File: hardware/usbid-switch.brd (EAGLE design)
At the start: 33 x 22.9 mm, 5 parts, among them J1 USB-MICRO-ZX80-B-5S, J2 USB-MICRO-105133-0011, SW1 SWITCH-SPDT-EG1215

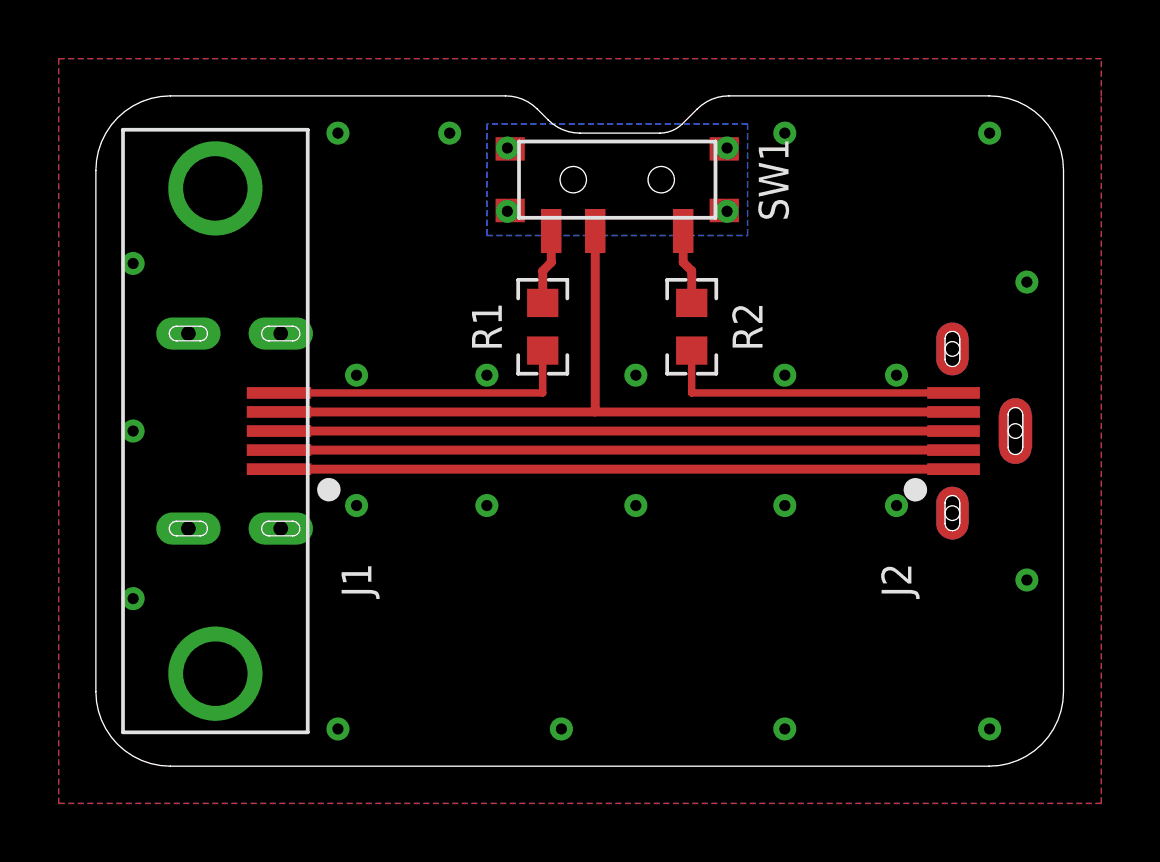
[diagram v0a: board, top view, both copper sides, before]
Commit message: Updated BOM attributes for currently available parts
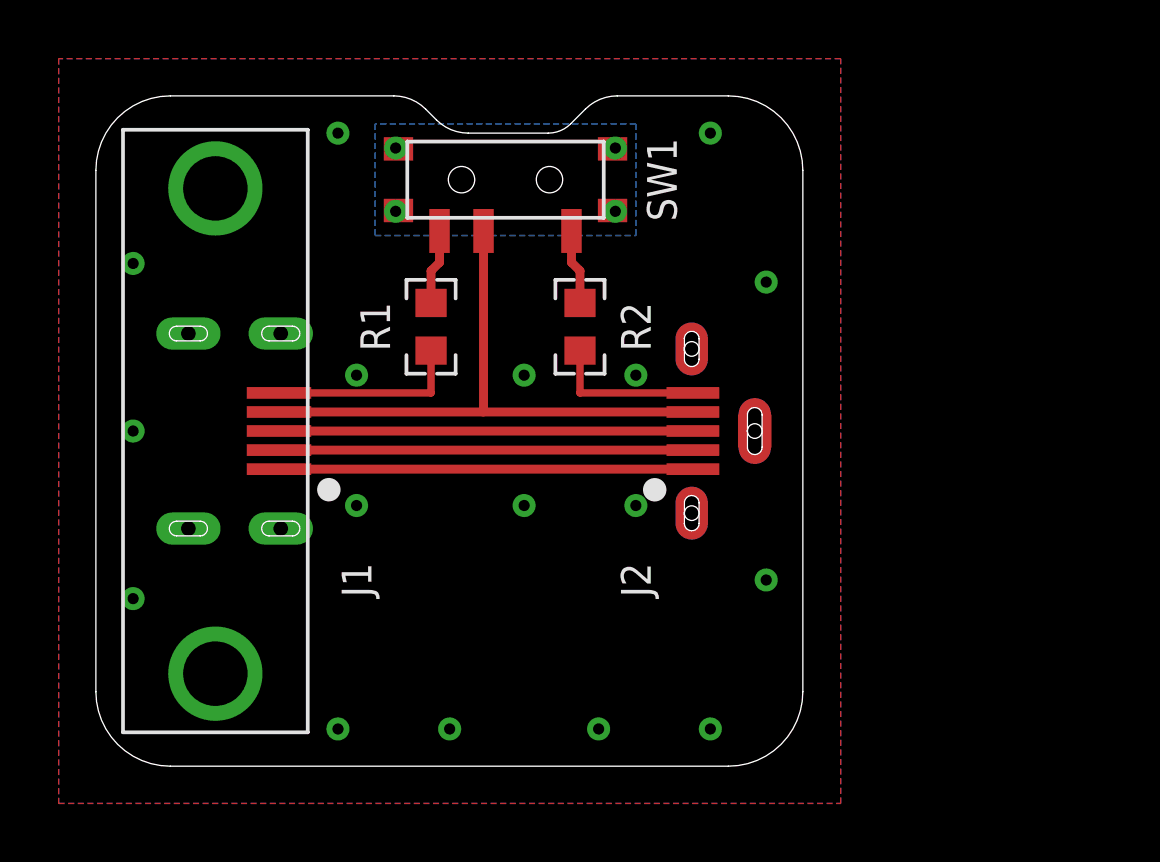
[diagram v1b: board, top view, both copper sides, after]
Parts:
- moved J2 8.89 mm to (21.6, 11.4)
- moved R1 3.81 mm to (11.4, 15.0)
- moved SW1 3.81 mm to (14.0, 20.0)
- moved R2 3.81 mm to (16.5, 15.0)
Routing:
- net GND: track 20.8 -> 11.9 mm, vias 23 -> 17
- net VBUS: track 23.0 -> 14.1 mm
- net ID: track 29.2 -> 20.3 mm
- net D-: track 23.0 -> 14.1 mm
- net D+: track 23.0 -> 14.1 mm
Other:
- board size 33 x 22.9 mm -> 24.1 x 22.9 mm
